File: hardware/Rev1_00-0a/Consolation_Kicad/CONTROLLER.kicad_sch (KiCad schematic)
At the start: 1 part, among them U2 RP2350A

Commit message: Update schematics, block diagram and pin mux (good progress G)
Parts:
- added C114, C126, C129, C131, C132, C133, C134, C140, C141, C142, C143, C144, C145, C149, C150, C151, C152, C228: 0.1u, footprint:CAP_NONPOL_0402, symbol KicadCompDb:Capacitors/CAP_CER_SMT_00001
- added C127, C128, C130, C139, C146, C147, C148, C153: 1u, footprint:CAP_NONPOL_0805, symbol KicadCompDb:Capacitors/CAP_CER_SMT_00002
- added C13, C14, C15: 10u, footprint:CAP_NONPOL_1210, symbol KicadCompDb:Capacitors/CAP_CER_SMT_00014
- added D2, D3: BAT42WS-TP, footprint:SOD-323, symbol KicadCompDb:Diodes/DIODE_00006
- added J11, J13: 5051101092, footprint:5051101092, symbol KicadCompDb:Connector/CONN_00005
- added J14, J15: SFV5R-2STBE1HLF, footprint:SFV5R-2ST, symbol KicadCompDb:Connector/CONN_00028
- added L2: AOTA-B201610S3R3-101-T, footprint:AOTA-B201610S3R3-101-T, symbol KicadCompDb:Inductor/IND_00011
- added R10, R9: 27R, footprint:RES_0402, symbol KicadCompDb:Resistors/RES_SMT_00036
- added R12: 100R, footprint:RES_0402, symbol KicadCompDb:Resistors/RES_SMT_00035
- added R128, R133, R134: 22R, footprint:RES_0402, symbol KicadCompDb:Resistors/RES_SMT_00015
- added R179, R180, R280: 10K, footprint:RES_0402, symbol KicadCompDb:Resistors/RES_SMT_00013
- added R181: 6K04, footprint:RES_0402, symbol KicadCompDb:Resistors/RES_SMT_00011
- added S1: KSR233G LFG, footprint:Y35A23310FPLFG, symbol KicadCompDb:Miscellaneous/MISC_00007
- added U7: ECS-2016MVQ-120-BP-TR, footprint:4-SMD_2mmx1_6mm, symbol KicadCompDb:Oscillator/OSC_00003
- added U8: GD25Q32CWIGR, footprint:WSON-8-EP, symbol KicadCompDb:Memory/MEMORY_00002
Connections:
- net at U2.21 (XIN): now also R128.2
- net SWDCLK: now reaches U2.24 (SWDCLK)
- net SWDIO: now reaches U2.25 (SWDIO)
- net ~{RP2350_RESET}: now reaches U2.26 (~{RESET})
- net ~{RP2350_RESET}: now also R280.2, U7.1 (EN)
- net at U2.51 (USB_DN): now also R10.2
- net at U2.52 (USB_DP): now also R9.2
- net at U2.55 (QSPI_SD3): now also U8.7 (~{HOLD}/IO3)
- net at U2.56 (QSPI_SCLK): now also R133.1
- net at U2.57 (QSPI_SD0): now also U8.5 (SI/IO0)
- net at U2.58 (QSPI_SD2): now also U8.3 (~{WP}/IO2)
- net at U2.59 (QSPI_SD1): now also U8.2 (SO/IO1)
- net at U2.60 (~{QSPI_SS}): now also D2.2 (A), D3.2 (A), U8.1 (~{CE})
- net 3V3: now reaches U2.1 (IOVDD)
- net 3V3: now also U2.11 (IOVDD), U2.20 (IOVDD), U2.30 (IOVDD), U2.38 (IOVDD), U2.45 (IOVDD), U2.49 (VREG_VIN), U2.53 (USB_OTP_VDD), U2.54 (QSPI_IOVDD), C126.2, C127.2, C128.2, C129.2, C14.2, C140.2, C141.2, C142.2, C143.2, C144.2, C145.2, C146.2, C147.2, C150.2, C151.2, C228.2, J11.1, J13.1, J14.1, J15.1, R12.1, R134.1, U7.4 (VDD), U8.8 (VDD)
- net 1V1_CORE: now reaches U2.23 (DVDD)
- net 1V1_CORE: now also U2.39 (DVDD), U2.50 (VREG_FB), U2.6 (DVDD), C13.2, C130.2, C131.2, C132.2, C133.2, C134.2, C139.2, C15.2, L2.1 (+)
- net at U2.44 (ADC_AVDD): now also C148.2, C149.2, R12.2
- net at U2.46 (VREG_AVDD): now also C152.2, C153.2, R134.2
- net GND: now reaches U2.47 (VREG_PGND)
- net GND: now also U2.61 (GND-EP), C114.1, C126.1, C127.1, C128.1, C129.1, C13.1, C130.1, C131.1, C132.1, C133.1, C134.1, C139.1, C14.1, C140.1, C141.1, C142.1, C143.1, C144.1, C145.1, C146.1, C147.1, C148.1, C149.1, C15.1, C150.1, C151.1, C152.1, C153.1, C228.1, J11.10, J13.10, J14.5, J15.5, R179.1, R180.1, R280.1, U7.2 (GND), U8.4 (GND), U8.9 (EP)
- net at U2.48 (VREG_LX): now also L2.2 (-)
- net at U2.36 (GPIO24): now also C114.2, R180.2, R181.1
- new net: R128.1, U7.3 (OUT)
- new net: R133.2, U8.6 (SCLK)
- new net: D3.1 (K), S1.2
- new net: R179.2, S1.1
- new net BTN_A: J13.5
- new net BTN_B: J13.6
- new net BTN_X: J13.7
- new net BTN_Y: J13.8
- new net CM5_USB3_1.USB_N: R10.1
- new net CM5_USB3_1.USB_P: R9.1
- new net DPAD_DOWN: J11.6
- new net DPAD_LEFT: J11.7
- new net DPAD_RIGHT: J11.8
- new net DPAD_UP: J11.5
- new net EXTRA: J15.4
- new net HOME: J14.4
- new net L_L1_TRIG: J14.2
- new net L_L2_TRIG: J14.3
- new net L_THUMBST_SW: J11.4
- new net L_THUMBST_X: J11.2
- new net L_THUMBST_Y: J11.3
- new net RP2350_USB_VBUS: R181.2
- new net R_L1_TRIG: J15.2
- new net R_L2_TRIG: J15.3
- new net R_THUMBST_SW: J13.4
- new net R_THUMBST_X: J13.2
- new net R_THUMBST_Y: J13.3
- new net SELECT: J13.9
- new net START: J11.9
- new net ~{RP2350_USB_BOOT}: D2.1 (K)
- no-connect marks 0 -> 1
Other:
- note added: "Controller - L"
- note added: "Controller - R"
- note added: "Internal PU 4K7 QSPI_IOVDD"
- note added: "Pull low before power-up to boot from USB"
- note added: "Resistors are 1% 1/16W 0402 unless otherwise noted Capacitors are 10% 50V X7R 0402 unless otherwise noted"
- note added: "Triggers - L"
- note added: "Triggers - R"
- moved on the sheet: U2A, U2B, U2C, U2D

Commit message: Update PinMux & Schematics
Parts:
- removed C228: 0.1u, footprint:CAP_NONPOL_0402, symbol KicadCompDb:Capacitors/CAP_CER_SMT_00001
- removed R128: 22R, footprint:RES_0402, symbol KicadCompDb:Resistors/RES_SMT_00015
- removed U7: ECS-2016MVQ-120-BP-TR, footprint:4-SMD_2mmx1_6mm, symbol KicadCompDb:Oscillator/OSC_00003
- added C154, C155, C156, C157: 1u, footprint:CAP_NONPOL_0805, symbol KicadCompDb:Capacitors/CAP_CER_SMT_00002
- added C16, C17: 15p, footprint:CAP_NONPOL_0402, symbol KicadCompDb:Capacitors/CAP_CER_SMT_00019
- added R11: 0R, footprint:RES_0603, symbol KicadCompDb:Resistors/RES_SMT_00021
- added R13, R14, R15, R16, R17: 10K, footprint:RES_ARRAY_4_1206, symbol KicadCompDb:Resistors/RES_SMT_00037
- added R135: 22R, footprint:RES_0402, symbol KicadCompDb:Resistors/RES_SMT_00015
- added R150, R157, R159: 10K, footprint:RES_0402, symbol KicadCompDb:Resistors/RES_SMT_00013
- added R18, R20: 100R, footprint:RES_0402, symbol KicadCompDb:Resistors/RES_SMT_00035
- added Y1: 12MHz 10pF, footprint:4-SMD_3_2mmx2_5mm, symbol KicadCompDb:Crystals/CRYSTAL_00004
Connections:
- net BTN_A is gone; now on net R_BTN_A: J13.5
- net BTN_B is gone; now on net R_BTN_B: J13.6
- net BTN_X is gone; now on net R_BTN_X: J13.7
- net BTN_Y is gone; now on net R_BTN_Y: J13.8
- net DPAD_DOWN is gone; now on net L_DPAD_DOWN: J11.6
- net DPAD_LEFT is gone; now on net L_DPAD_LEFT: J11.7
- net DPAD_RIGHT is gone; now on net L_DPAD_RIGHT: J11.8
- net DPAD_UP is gone; now on net L_DPAD_UP: J11.5
- net EXTRA is gone; now on net R_EXTRA: J15.4
- net HOME is gone; now on net L_HOME: J14.4
- net SELECT is gone; now on net R_SELECT: J13.9
- net START is gone; now on net L_START: J11.9
- net 3V3: now also C154.2, C155.2, C156.2, C157.2, R13.5, R13.6, R13.7, R13.8, R14.5, R14.6, R14.7, R14.8, R15.5, R15.6, R15.7, R15.8, R150.2, R157.2, R159.2, R16.5, R16.6, R16.7, R16.8, R17.5, R17.6, R17.7, R17.8
- net GND: now also C154.1, C155.1, C156.1, C157.1, C16.1, C17.1, Y1.2 (GND), Y1.4 (GND)
- net L_L1_TRIG: now also U2.12 (GPIO8), R13.1
- net L_L2_TRIG: now also U2.13 (GPIO9), R13.2
- net L_THUMBST_SW: now also U2.35 (GPIO23), R157.1
- net L_THUMBST_X: now also U2.40 (GPIO26_ADC0), R17.1
- net L_THUMBST_Y: now also U2.41 (GPIO27_ADC1), R17.2
- net R_L1_TRIG: now also U2.14 (GPIO10), R13.3
- net R_L2_TRIG: now also U2.15 (GPIO11), R13.4
- net R_THUMBST_SW: now also U2.37 (GPIO25), R159.1
- net R_THUMBST_X: now also U2.42 (GPIO28_ADC2), R17.3
- net R_THUMBST_Y: now also U2.43 (GPIO29_ADC3), R17.4
- net SWDCLK: now also R18.1; no longer U2.24 (SWDCLK)
- net SWDIO: now also R20.1; no longer U2.25 (SWDIO)
- net at U2.21 (XIN): now also C17.2, Y1.3 (XO)
- net at U2.22 (XOUT): now also R11.1
- net R_EXTRA: now reaches U2.10 (GPIO7)
- net R_EXTRA: now also R15.2
- net L_DPAD_UP: now reaches U2.16 (GPIO12)
- net L_DPAD_UP: now also R14.1
- net L_DPAD_DOWN: now reaches U2.17 (GPIO13)
- net L_DPAD_DOWN: now also R14.2
- net L_DPAD_LEFT: now reaches U2.18 (GPIO14)
- net L_DPAD_LEFT: now also R14.3
- net L_DPAD_RIGHT: now reaches U2.19 (GPIO15)
- net L_DPAD_RIGHT: now also R14.4
- net at U2.2 (GPIO0): now also R135.1
- net RP2350_RXD0: now reaches U2.3 (GPIO1)
- net RP2350_RXD0: now also R150.1
- net I2C2.I2C_SDA: now reaches U2.4 (GPIO2)
- net I2C2.I2C_SCL: now reaches U2.5 (GPIO3)
- net L_HOME: now reaches U2.9 (GPIO6)
- net L_HOME: now also R15.1
- net L_START: now reaches U2.27 (GPIO16)
- net L_START: now also R15.3
- net R_SELECT: now reaches U2.28 (GPIO17)
- net R_SELECT: now also R15.4
- net R_BTN_A: now reaches U2.31 (GPIO19)
- net R_BTN_A: now also R16.1
- net R_BTN_B: now reaches U2.32 (GPIO20)
- net R_BTN_B: now also R16.2
- net R_BTN_X: now reaches U2.33 (GPIO21)
- net R_BTN_X: now also R16.3
- net R_BTN_Y: now reaches U2.34 (GPIO22)
- net R_BTN_Y: now also R16.4
- new net: R18.2, U2.24 (SWDCLK)
- new net: R20.2, U2.25 (SWDIO)
- new net: C16.2, R11.2, Y1.1 (XI)
- new net RP2350_TXD0: R135.2
- no-connect marks 1 -> 3
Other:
- note added: "Adjust buttons mapping to ease layout"
- note added: "PU'd at DSI bridge"
- moved on the sheet: C114, C128, C129, C13, C130, C131, C132, C133, C134, C139, C14, C140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

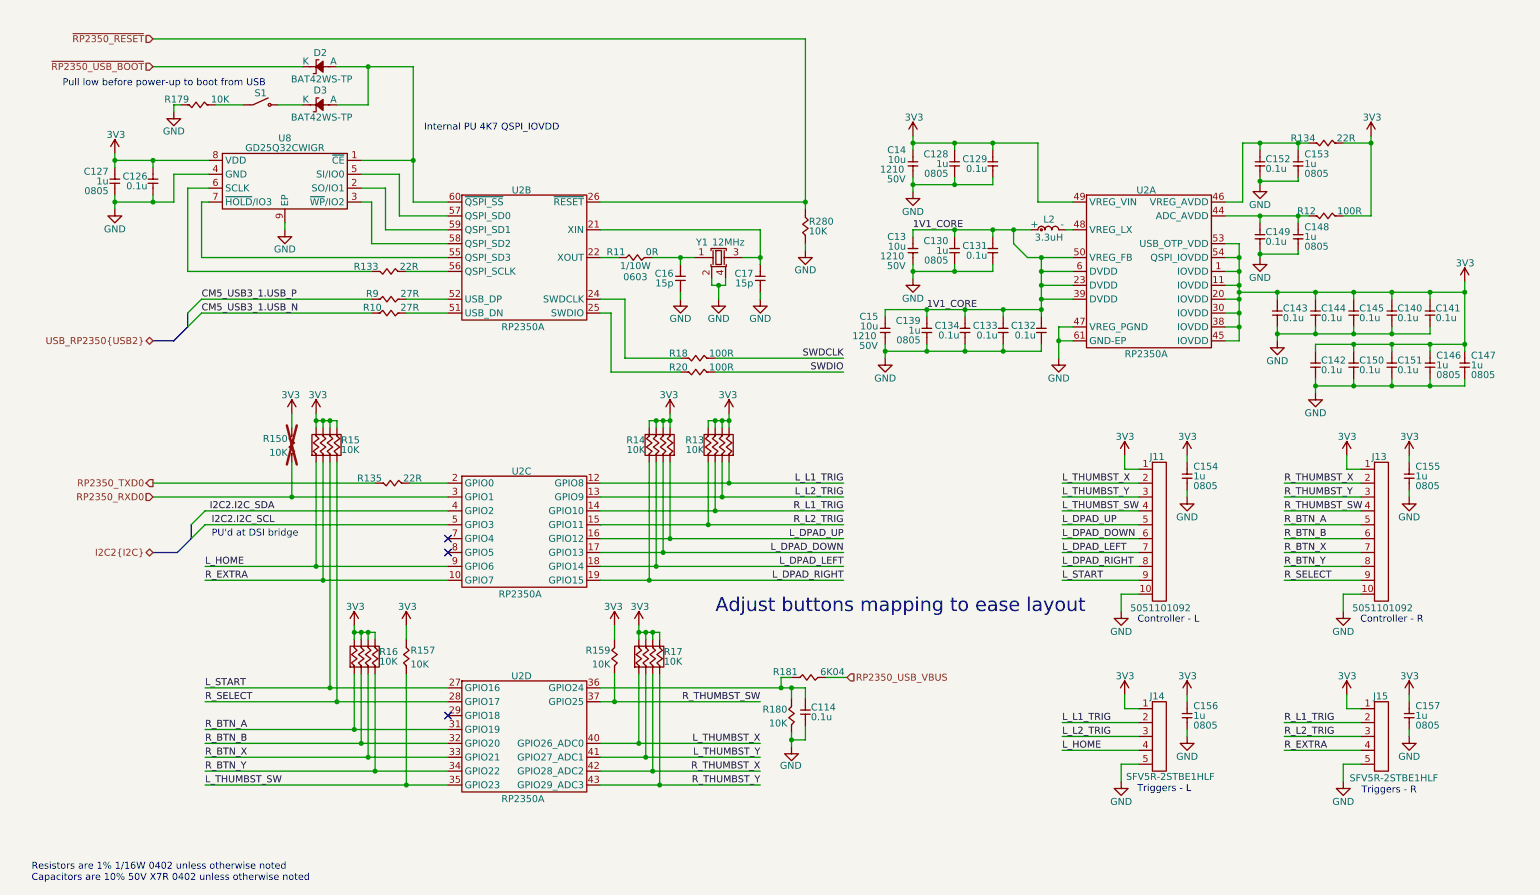
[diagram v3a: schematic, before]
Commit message: Work on ConJoy [Consolation Joycon] Work on Consolation [Console Emulation]
- Adjust controller pinout
- Design controller for 1-PCB fits both side (reversible design for L-R controller)
- Preliminary PCB for 3d modeling
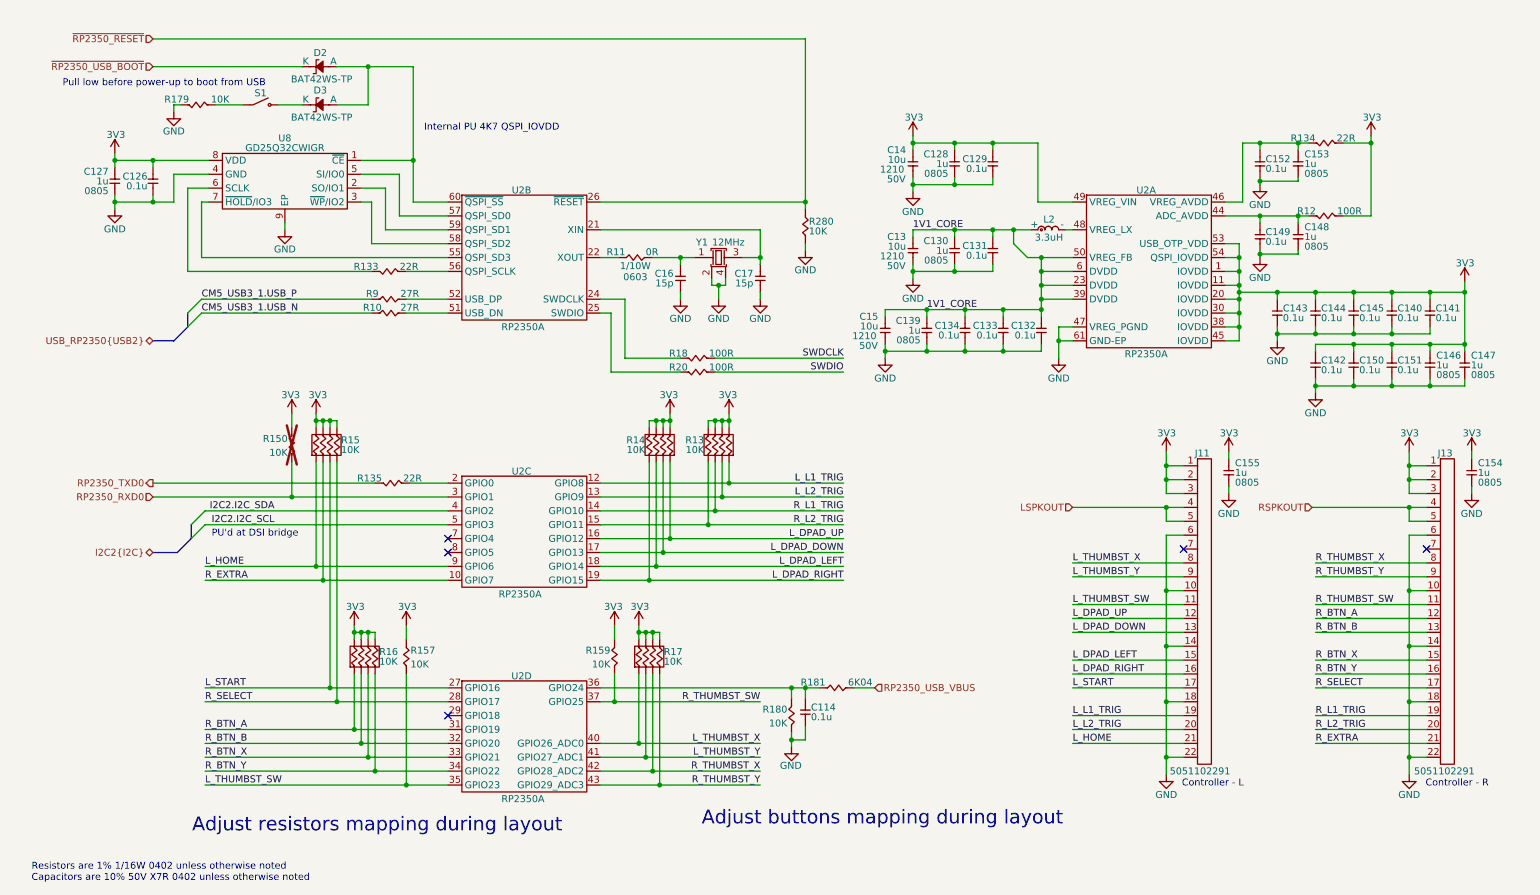
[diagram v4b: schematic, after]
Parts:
- removed C156, C157: 1u, footprint:CAP_NONPOL_0805, symbol KicadCompDb:Capacitors/CAP_CER_SMT_00002
- removed J11, J13: 5051101092, footprint:5051101092, symbol KicadCompDb:Connector/CONN_00005
- removed J14, J15: SFV5R-2STBE1HLF, footprint:SFV5R-2ST, symbol KicadCompDb:Connector/CONN_00028
- added J11, J13: 5051102291, footprint:5051102291, symbol KicadCompDb:Connector/CONN_00006
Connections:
- net 3V3: now also J11.1, J11.2, J11.3, J13.1, J13.2, J13.3
- net GND: now also J11.10, J11.14, J11.18, J11.22, J11.6, J13.10, J13.14, J13.18, J13.22, J13.6
- net L_DPAD_DOWN: now also J11.13
- net L_DPAD_LEFT: now also J11.15
- net L_DPAD_RIGHT: now also J11.16
- net L_DPAD_UP: now also J11.12
- net L_HOME: now also J11.21
- net L_L1_TRIG: now also J11.19
- net L_L2_TRIG: now also J11.20
- net L_START: now also J11.17
- net L_THUMBST_SW: now also J11.11
- net L_THUMBST_X: now also J11.8
- net L_THUMBST_Y: now also J11.9
- net R_BTN_A: now also J13.12
- net R_BTN_B: now also J13.13
- net R_BTN_X: now also J13.15
- net R_BTN_Y: now also J13.16
- net R_EXTRA: now also J13.21
- net R_L1_TRIG: now also J13.19
- net R_L2_TRIG: now also J13.20
- net R_SELECT: now also J13.17
- net R_THUMBST_SW: now also J13.11
- net R_THUMBST_X: now also J13.8
- net R_THUMBST_Y: now also J13.9
- new net LSPKOUT: J11.4, J11.5
- new net RSPKOUT: J13.4, J13.5
- no-connect marks 3 -> 5
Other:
- note added: "Adjust buttons mapping during layout"
- note added: "Adjust resistors mapping during layout"
- note removed: "Adjust buttons mapping to ease layout"
- note removed: "Triggers - L"
- note removed: "Triggers - R"
- moved on the sheet: C154, C155, R181

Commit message: ConJoy mostly ready for alpha prototype. Confirm few other potential tweaks at 3d printing
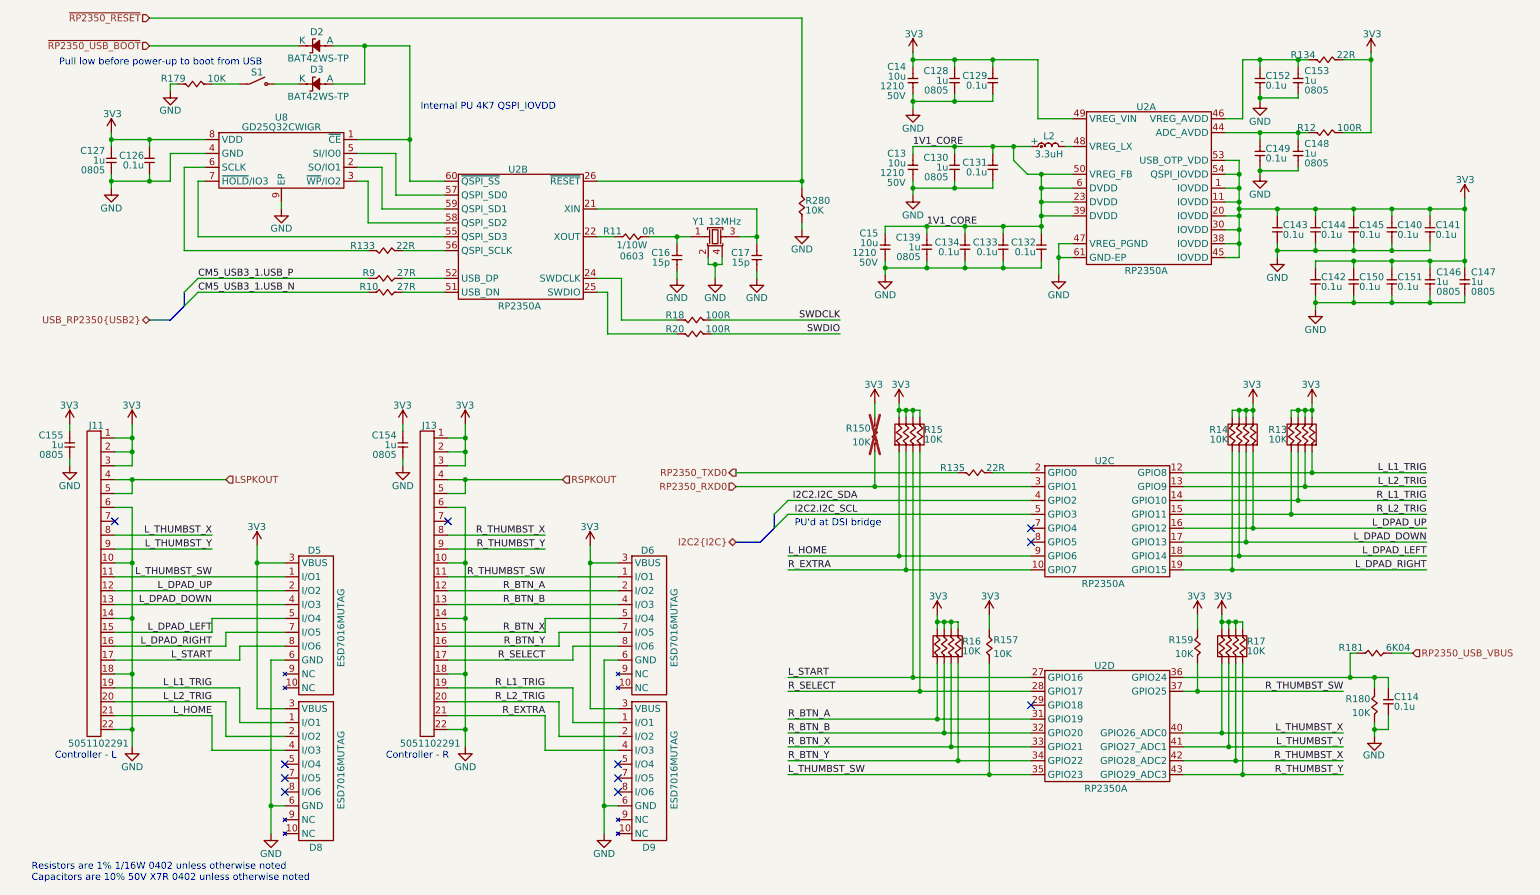
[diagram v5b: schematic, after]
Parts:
- added D5, D6, D8, D9: ESD7016MUTAG, footprint:UDFN8, symbol KicadCompDb:ESD Diodes/ESD_DIODE_00001
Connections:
- net 3V3: now also D5.3 (VBUS), D6.3 (VBUS), D8.3 (VBUS), D9.3 (VBUS)
- net GND: now also D5.6 (GND), D6.6 (GND), D8.6 (GND), D9.6 (GND)
- net L_DPAD_DOWN: now also D5.4 (I/O3)
- net L_DPAD_LEFT: now also D5.5 (I/O4)
- net L_DPAD_RIGHT: now also D5.7 (I/O5)
- net L_DPAD_UP: now also D5.2 (I/O2)
- net L_HOME: now also D8.4 (I/O3)
- net L_L1_TRIG: now also D8.1 (I/O1)
- net L_L2_TRIG: now also D8.2 (I/O2)
- net L_START: now also D5.8 (I/O6)
- net L_THUMBST_SW: now also D5.1 (I/O1)
- net R_BTN_A: now also D6.2 (I/O2)
- net R_BTN_B: now also D6.4 (I/O3)
- net R_BTN_X: now also D6.5 (I/O4)
- net R_BTN_Y: now also D6.7 (I/O5)
- net R_EXTRA: now also D9.4 (I/O3)
- net R_L1_TRIG: now also D9.1 (I/O1)
- net R_L2_TRIG: now also D9.2 (I/O2)
- net R_SELECT: now also D6.8 (I/O6)
- net R_THUMBST_SW: now also D6.1 (I/O1)
- no-connect marks 5 -> 11
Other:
- note removed: "Adjust buttons mapping during layout"
- note removed: "Adjust resistors mapping during layout"
- moved on the sheet: C114, C126, C127, C128, C129, C13, C130, C131, C132, C133, C134, C139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

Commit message: Work on block diagram and top-level schematic sheet Work on PinMux
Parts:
- removed C114: 0.1u, footprint:CAP_NONPOL_0402, symbol KicadCompDb:Capacitors/CAP_CER_SMT_00001
- removed R180: 10K, footprint:RES_0402, symbol KicadCompDb:Resistors/RES_SMT_00013
- removed R181: 6K04, footprint:RES_0402, symbol KicadCompDb:Resistors/RES_SMT_00011
- added R160, R281: 10K, footprint:RES_0402, symbol KicadCompDb:Resistors/RES_SMT_00013
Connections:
- net 3V3: now also R281.2
- net GND: now also R160.1
- net RP2350_USB_VBUS: now also U2.36 (GPIO24), R160.2
- net at D2.2 (A), D3.2 (A), U2.60 (~{QSPI_SS})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: now also R281.1
